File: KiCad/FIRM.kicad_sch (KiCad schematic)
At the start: 95 parts, among them J1 Conn_01x02_Pin, J2 DM3CS-SF, J5 USB_C_Receptacle_USB2.0_16P, Q2 IRLML6402, SW1 PTS815, U1 STM32F405RGTx, U2 MIC5219-3.3YM5, U7 W25Q128JVS, X2 32.768khz, Y1 12 MHz

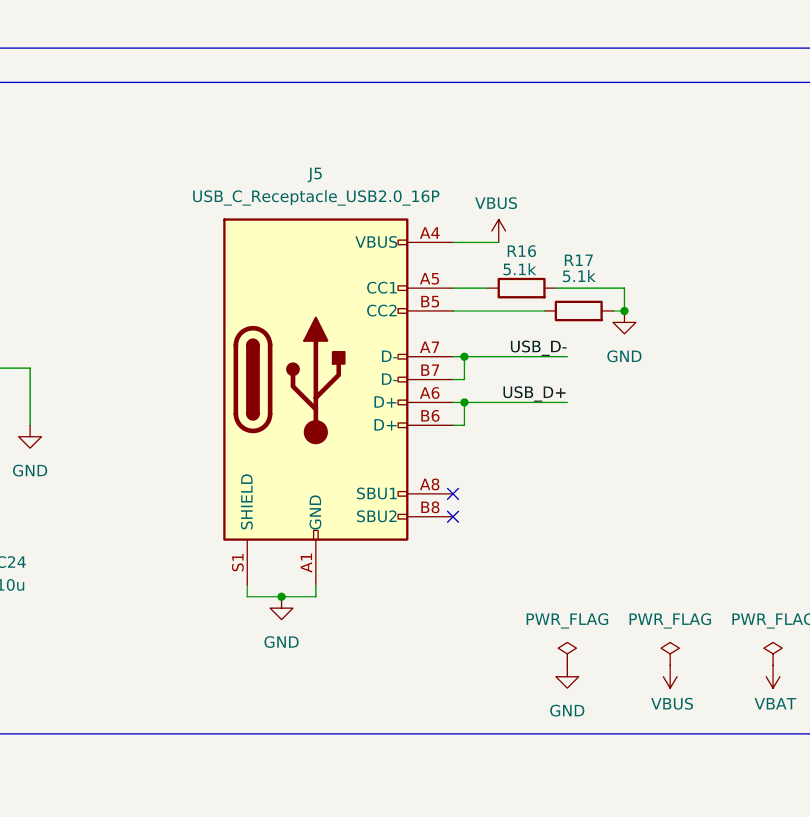
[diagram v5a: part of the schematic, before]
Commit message: Created Footprint and Symbol for the USBC we picked out.
I had to make the footprint and symbol because they weren't available online. Look over the shield pads and the diameter of the 2 circles (diameter is 1.2mm but it looks smaller on the datasheet)
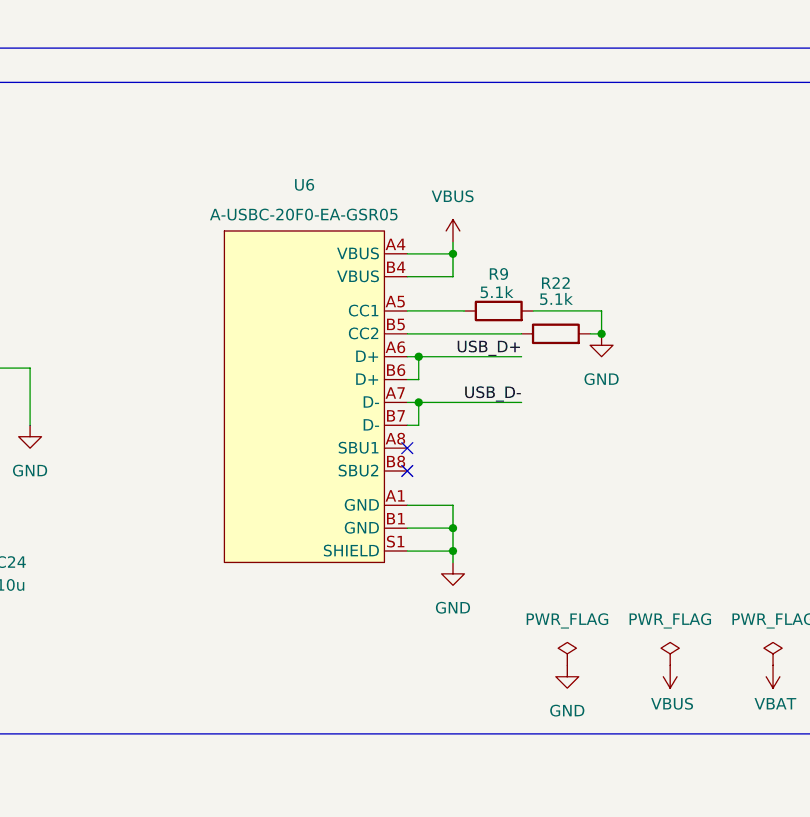
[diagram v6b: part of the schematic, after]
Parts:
- removed J5: USB_C_Receptacle_USB2.0_16P, Connector_USB:USB_C_Receptacle_Amphenol_124019772112A, symbol Connector:USB_C_Receptacle_USB2.0_16P
- removed R16, R17: 5.1k, Resistor_SMD:R_0603_1608Metric, symbol Device:R
- added R22, R9: 5.1k, Resistor_SMD:R_0603_1608Metric, symbol Device:R
- added U6: A-USBC-20F0-EA-GSR05, connectors:A-USBC-20F0-EA-GSR05, symbol connectors:A-USBC-20F0-EA-GSR05
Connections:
- net GND: now also R22.2, R9.2, U6.A1 (GND), U6.B1 (GND), U6.S1 (SHIELD)
- net USB_D+: now also U6.A6 (D+), U6.B6 (D+)
- net USB_D-: now also U6.A7 (D-), U6.B7 (D-)
- net VBUS: now also U6.A4 (VBUS), U6.B4 (VBUS)
- new net: R9.1, U6.A5 (CC1)
- new net: R22.1, U6.B5 (CC2)

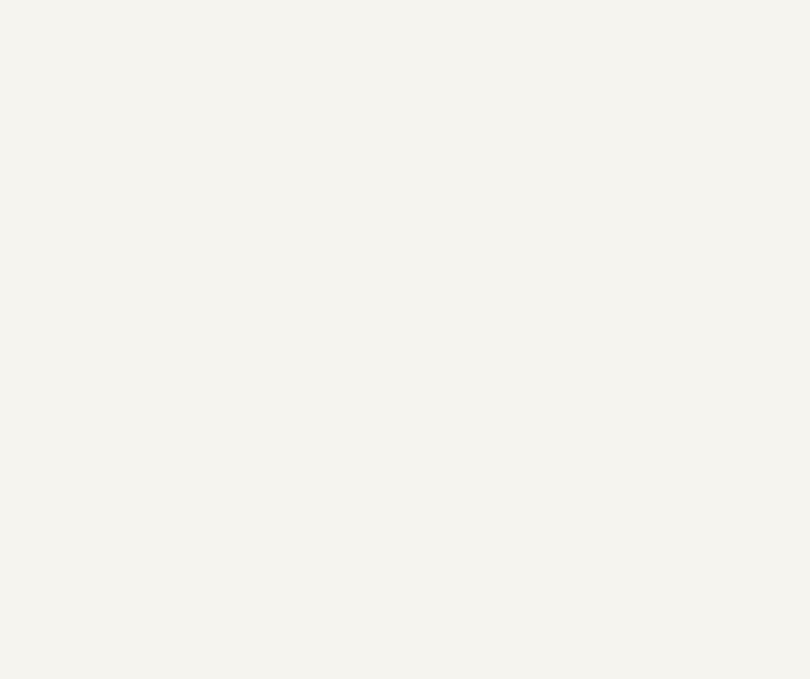
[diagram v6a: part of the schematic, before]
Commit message: Reconfigure PCB to 30.5mm FC mounting hole layout
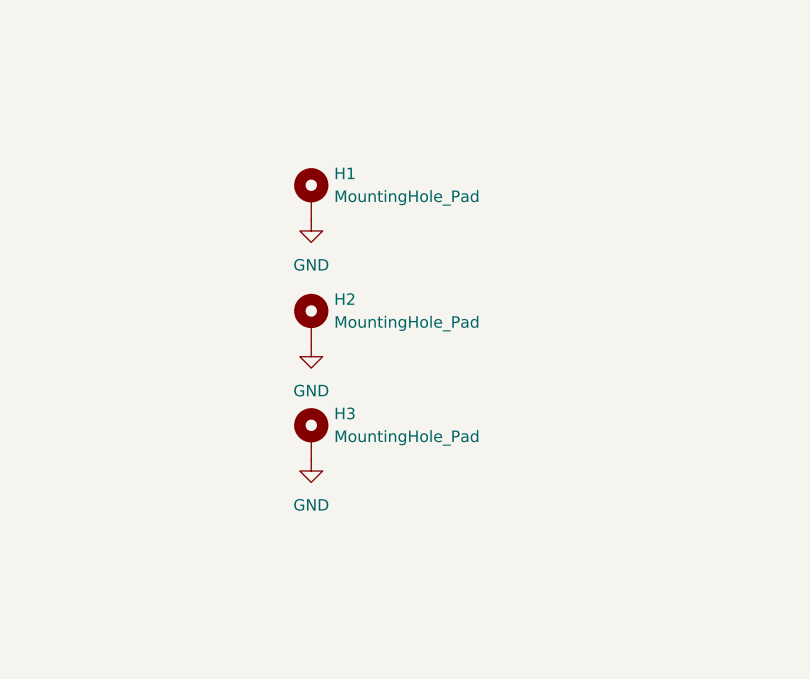
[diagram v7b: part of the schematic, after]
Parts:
- added H1, H2, H3: MountingHole_Pad, MountingHole:MountingHole_3.2mm_M3_DIN965_Pad, symbol Mechanical:MountingHole_Pad
- U3: footprint ICM-45686:IC_ICM-45686 -> sensors:IC_ICM-45686
- U4: footprint MMC5983MA:PQFN50P300X300X100-16N -> sensors:IC_MMC5983MA
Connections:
- net GND: now also H1.1, H2.1, H3.1

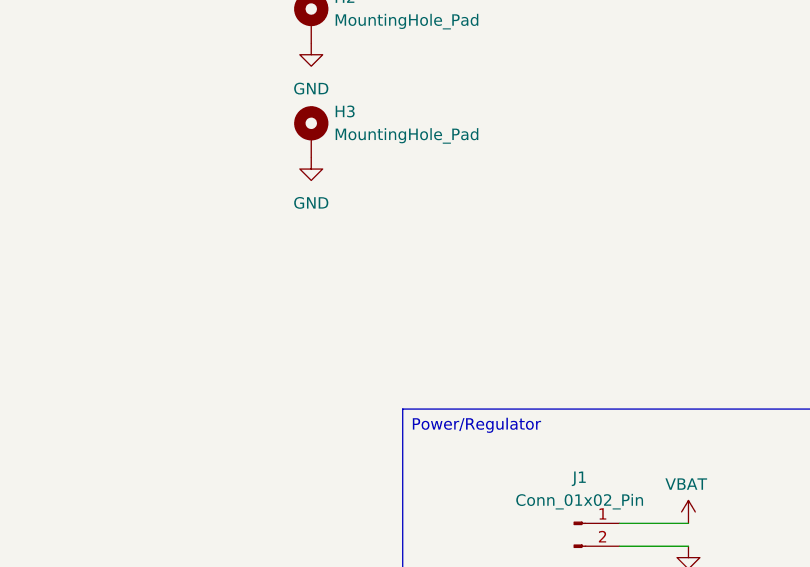
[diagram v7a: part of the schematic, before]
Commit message: Use 4 M3 mounting holes
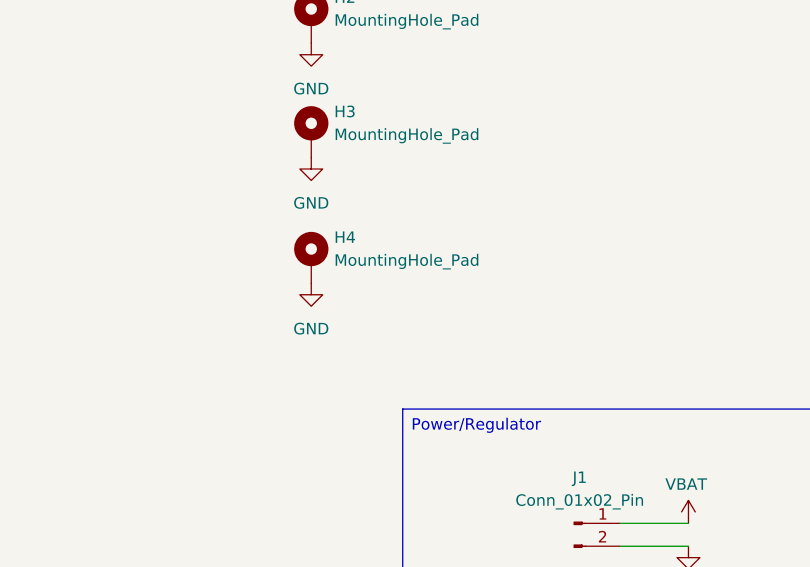
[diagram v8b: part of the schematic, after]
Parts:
- added H4: MountingHole_Pad, MountingHole:MountingHole_3.2mm_M3_Pad_Via, symbol Mechanical:MountingHole_Pad
- H1, H2, H3: footprint MountingHole:MountingHole_3.2mm_M3_DIN965_Pad -> MountingHole:MountingHole_3.2mm_M3_Pad_Via
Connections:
- net GND: now also H4.1
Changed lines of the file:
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@@
 	)
 	(symbol
+		(lib_id "Mechanical:MountingHole_Pad")
+		(at 227.33 153.67 0)
+		(unit 1)
+		(exclude_from_sim no)
+		(in_bom no)
+		(on_board yes)
+		(dnp no)
+		(fields_autoplaced yes)
+		(property "Reference" "H4"
+			(at 229.87 151.1299 0)
+			(effects
+				(font
+					(size 1.27 1.27)
+				)
+				(justify left)
+			)
+		)
+		(property "Value" "MountingHole_Pad"
+			(at 229.87 153.6699 0)
+			(effects
+				(font
+					(size 1.27 1.27)
+				)
+				(justify left)
+			)
+		)
+		(property "Footprint" "MountingHole:MountingHole_3.2mm_M3_Pad_Via"
+			(at 227.33 153.67 0)
+			(effects
+				(font
+					(size 1.27 1.27)
+				)
+				(hide yes)
+			)
+		)
+		(property "Datasheet" "~"
+			(at 227.33 153.67 0)
+			(effects
+				(font
+					(size 1.27 1.27)
+				)
+				(hide yes)
+			)
+		)
+		(property "Description" "Mounting Hole with connection"
+			(at 227.33 153.67 0)
+			(effects
+				(font
+					(size 1.27 1.27)
+				)
+				(hide yes)
+			)
+		)
+		(pin "1"
+		)
+		(instances
+			(project "FIRM"
+				(path "/d3f8a00a-ef65-439d-87f3-373a106a7ddb"
+					(reference "H4")
+					(unit 1)
+				)
+			)
+		)
+	)
+	(symbol
 		(lib_id "Connector:TestPoint")
 		(at 191.77 215.9 270)
@@
 			)
 		)
-		(property "Footprint" "MountingHole:MountingHole_3.2mm_M3_DIN965_Pad"
+		(property "Footprint" "MountingHole:MountingHole_3.2mm_M3_Pad_Via"
 			(at 227.33 113.03 0)
 			(effects
@@
 	)
 	(symbol
+		(lib_id "power:GND")
+		(at 227.33 156.21 0)
+		(unit 1)
+		(exclude_from_sim no)
+		(in_bom yes)
+		(on_board yes)
+		(dnp no)
+		(fields_autoplaced yes)
+		(property "Reference" "#PWR056"
+			(at 227.33 162.56 0)
+			(effects
+				(font
+					(size 1.27 1.27)
+				)
+				(hide yes)
+			)
+		)
+		(property "Value" "GND"
+			(at 227.33 161.29 0)
+			(effects
+				(font
+					(size 1.27 1.27)
+				)
+			)
+		)
+		(property "Footprint" ""
+			(at 227.33 156.21 0)
+			(effects
+				(font
+					(size 1.27 1.27)
+				)
+				(hide yes)
+			)
+		)
+		(property "Datasheet" ""
+			(at 227.33 156.21 0)
+			(effects
+				(font
+					(size 1.27 1.27)
+				)
+				(hide yes)
+			)
+		)
+		(property "Description" "Power symbol creates a global label with name \"GND\" , ground"
+			(at 227.33 156.21 0)
+			(effects
+				(font
+					(size 1.27 1.27)
+				)
+				(hide yes)
+			)
+		)
+		(pin "1"
+		)
+		(instances
+			(project "FIRM"
+				(path "/d3f8a00a-ef65-439d-87f3-373a106a7ddb"
+					(reference "#PWR056")
+					(unit 1)
+				)
+			)
+		)
+	)
+	(symbol
 		(lib_id "Device:C")
 		(at 73.66 130.81 0)
@@
 			)
 		)
-		(property "Footprint" "MountingHole:MountingHole_3.2mm_M3_DIN965_Pad"
+		(property "Footprint" "MountingHole:MountingHole_3.2mm_M3_Pad_Via"
 			(at 227.33 127 0)
 			(effects
@@
 			)
 		)
-		(property "Footprint" "MountingHole:MountingHole_3.2mm_M3_DIN965_Pad"
+		(property "Footprint" "MountingHole:MountingHole_3.2mm_M3_Pad_Via"
 			(at 227.33 139.7 0)
 			(effects
